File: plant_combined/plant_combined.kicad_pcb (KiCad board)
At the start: 4 copper layers, 68.6 x 58.4 mm, 72 parts, among them J1 SMA-J-P-H-ST-EM1, J2 PJ-002AH, J3 Conn_01x02, U1 SI5351A-B-GT, U10 ZXBM5210-SP-13, U2 OLED_DISP, U3 TDC7200PWR, U4 LMV7219M7, U5 74AC14SC, U6 ESD7002, U7 NCV8163ASN330T1G, U8 PicoW, U9 AP62200WU-7, Y1 Crystal_GND24

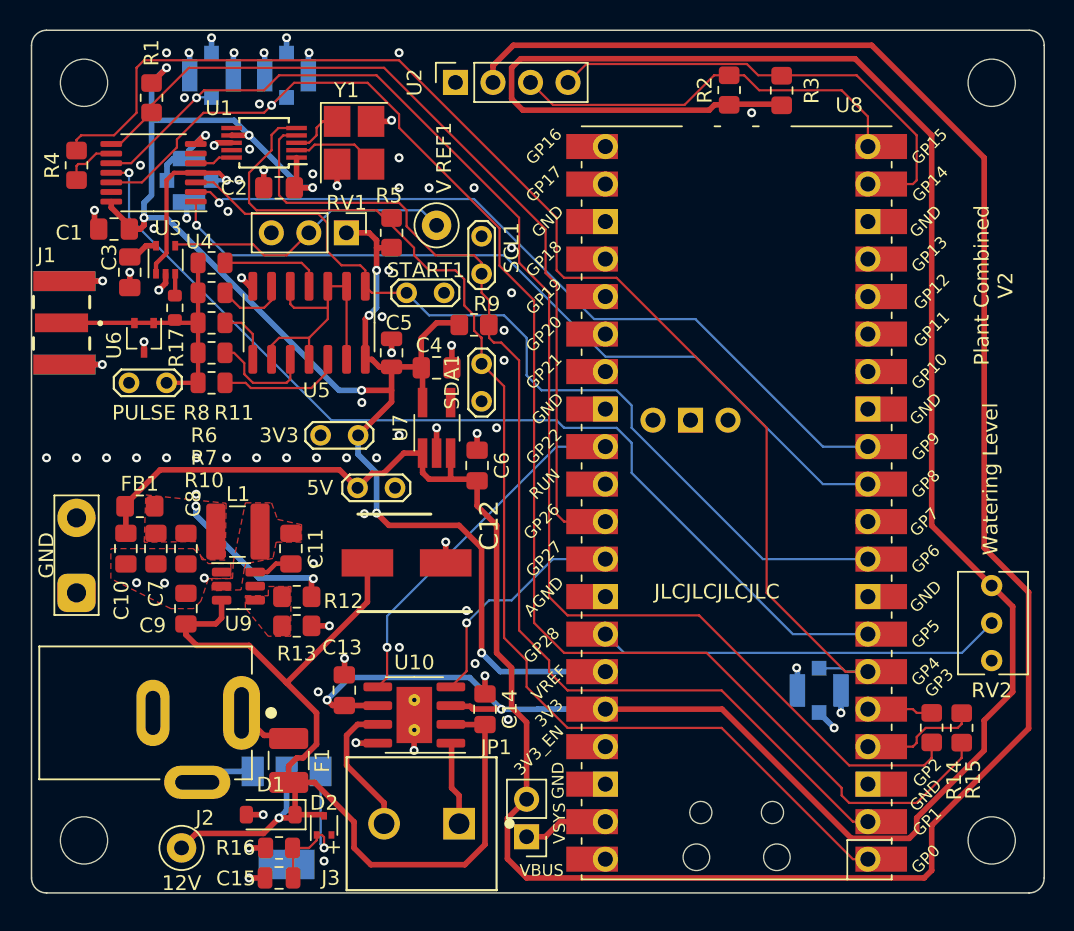
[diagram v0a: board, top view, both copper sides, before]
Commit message: Trying to clean up pulse trace
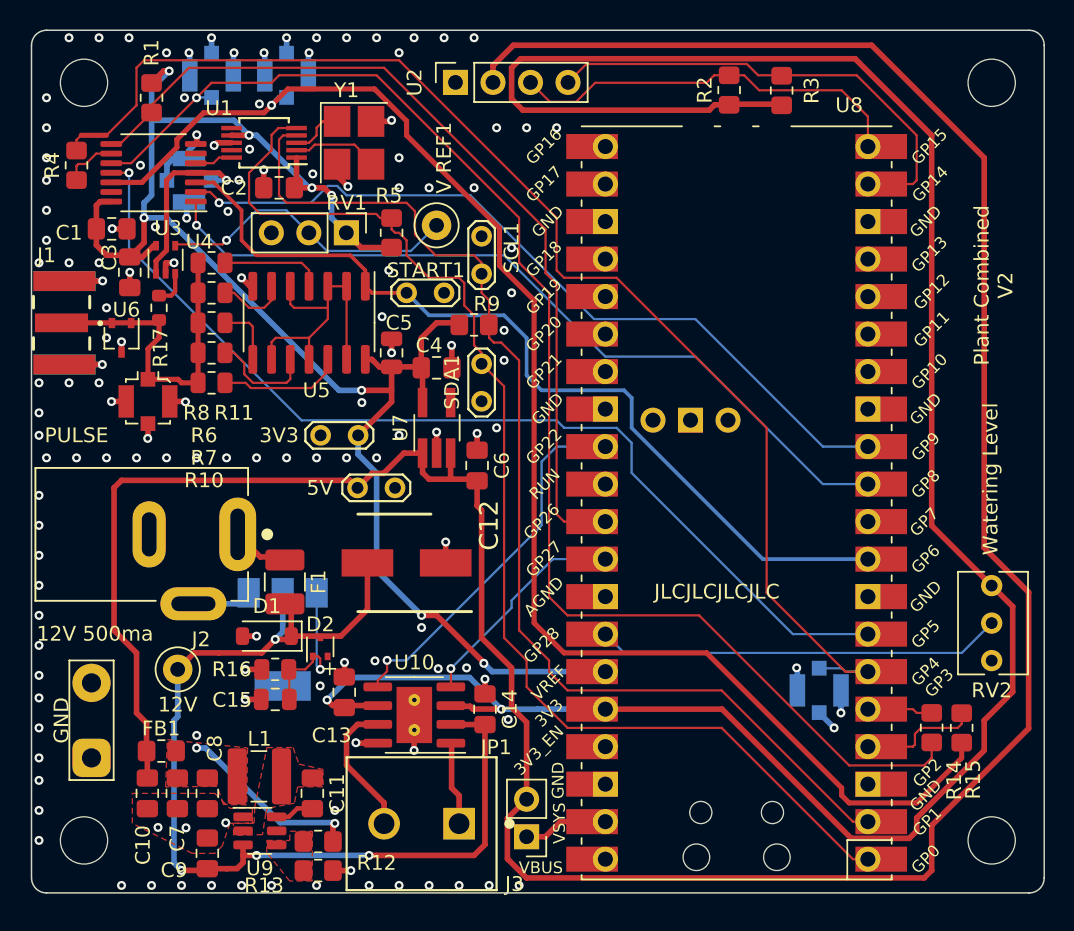
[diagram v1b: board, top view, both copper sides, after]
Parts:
- TP1: footprint Library:TestPoint_2Pads_Pitch2.54mm_Drill1mm -> Connector_Coaxial:U.FL_Molex_MCRF_73412-0110_Vertical
- moved C10 16.6 mm to (44.4, 116.7)
- moved C11 16.6 mm to (55.6, 116.7)
- moved C7 16.6 mm to (46.5, 116.7)
- moved C8 16.6 mm to (48.5, 116.7)
- moved C9 16.6 mm to (48.5, 120.8)
- moved FB1 16.6 mm to (45.4, 113.8)
- moved R12 16.6 mm to (56.0, 120.0)
- moved U9 16.6 mm to (52.0, 119.2)
- moved L1 16.6 mm to (53.5, 115.5)
- moved R13 16.6 mm to (56.0, 121.9)
- moved C15 12.1 mm to (53.1, 110.3)
- moved D1 12.1 mm to (52.5, 106.1)
- moved D2 12.1 mm to (56.1, 106.8)
- moved D3 12.1 mm to (53.6, 106.3)
- moved F1 12.1 mm to (53.7, 102.4)
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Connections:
- TP1 pad 1: GND -> /tdr_sensor/PULSE
- TP1 pad 2: /tdr_sensor/PULSE -> GND
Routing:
- net +5V: track 178.9 -> 197.4 mm
- net +12P: track 75.6 -> 70.0 mm, vias 1 -> 4
- net /tdr_sensor/PULSE: track 19.5 -> 22.5 mm
- net GND: track 62.3 -> 63.9 mm, vias 83 -> 138
- net TDC CSB: track 67.2 -> 68.3 mm
- net /5V_UNFILT: track 11.6 -> 12.8 mm
- net /AIN1: track 16.0 -> 15.1 mm
- net Net-(U4-+): track 1.53 -> 2.42 mm
- net /tdr_sensor/V ref: track 19.7 -> 20.6 mm, vias 0 -> 1
- net /AIN2: track 24.6 -> 25.4 mm
- net +3.3VA: track 116.3 -> 115.6 mm, vias 9 -> 8
- net TRIG: track 52.9 -> 53.7 mm
- net SDA: track 81.5 -> 82.0 mm

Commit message: Final tweak before release
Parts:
- removed R2, R3: 10K, Resistor_SMD:R_0805_2012Metric_Pad1.20x1.40mm_HandSolder
- MOSI1, SCLK1, STOP1, TP1, TP6: footprint Connector_Coaxial:U.FL_Molex_MCRF_73412-0110_Vertical -> Library:HIROSE_U.FL-R-SMT-1(01)
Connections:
- RV2 pad 1: +3.3V -> +3.3VA
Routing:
- net +3.3V: track 156.2 -> 27.5 mm
- net +5V: track 197.4 -> 136.3 mm, vias 0 -> 2
- net +3.3VA: track 115.6 -> 156.9 mm, vias 8 -> 9
- net Net-(U2-SCK): track 27.3 -> 49.5 mm
- net Net-(U2-SDA): track 32.6 -> 43.1 mm
- net GND: track 63.9 -> 56.7 mm, vias 138 -> 127
- net MISO: track 87.2 -> 91.3 mm
- net /AIN2: track 25.4 -> 24.6 mm
- net Net-(U8-GPIO28_ADC2): vias 0 -> 1
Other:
- board text removed: "+"

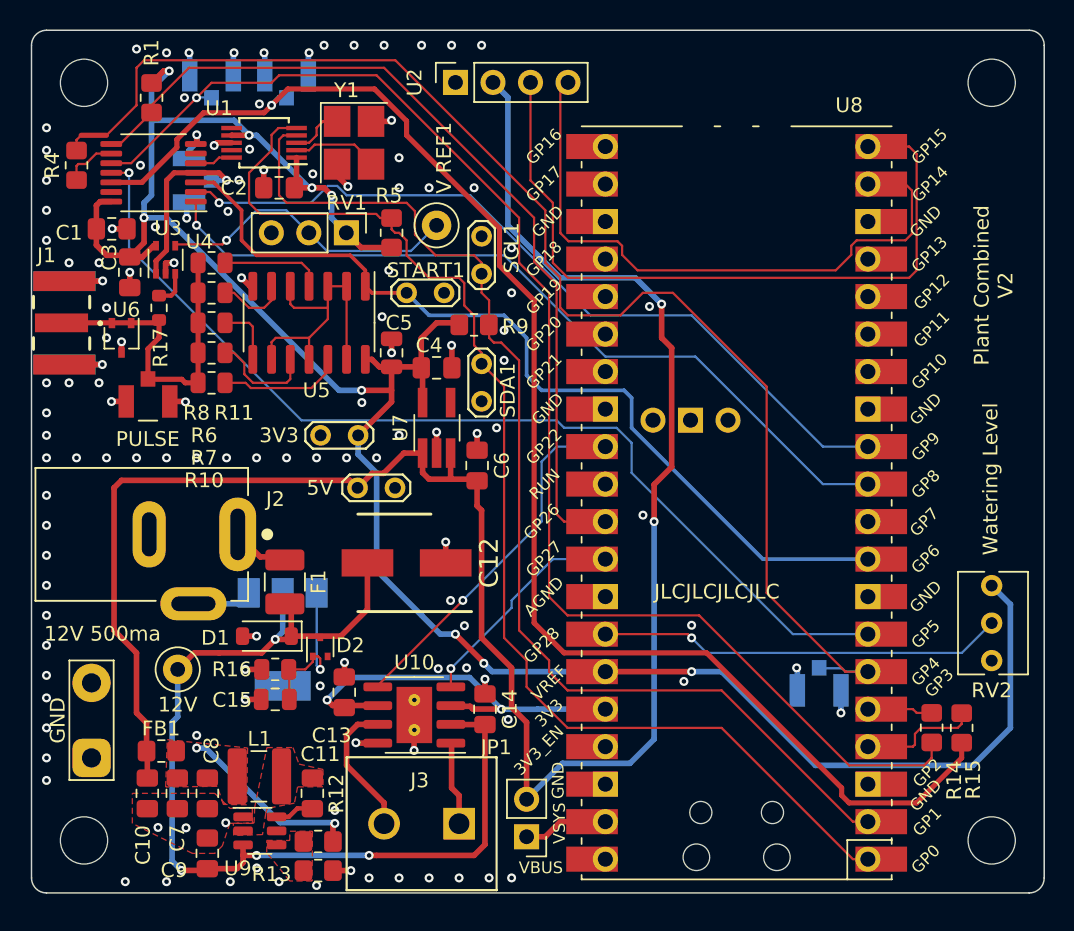
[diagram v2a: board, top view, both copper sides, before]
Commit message: Add pull-up to MISO
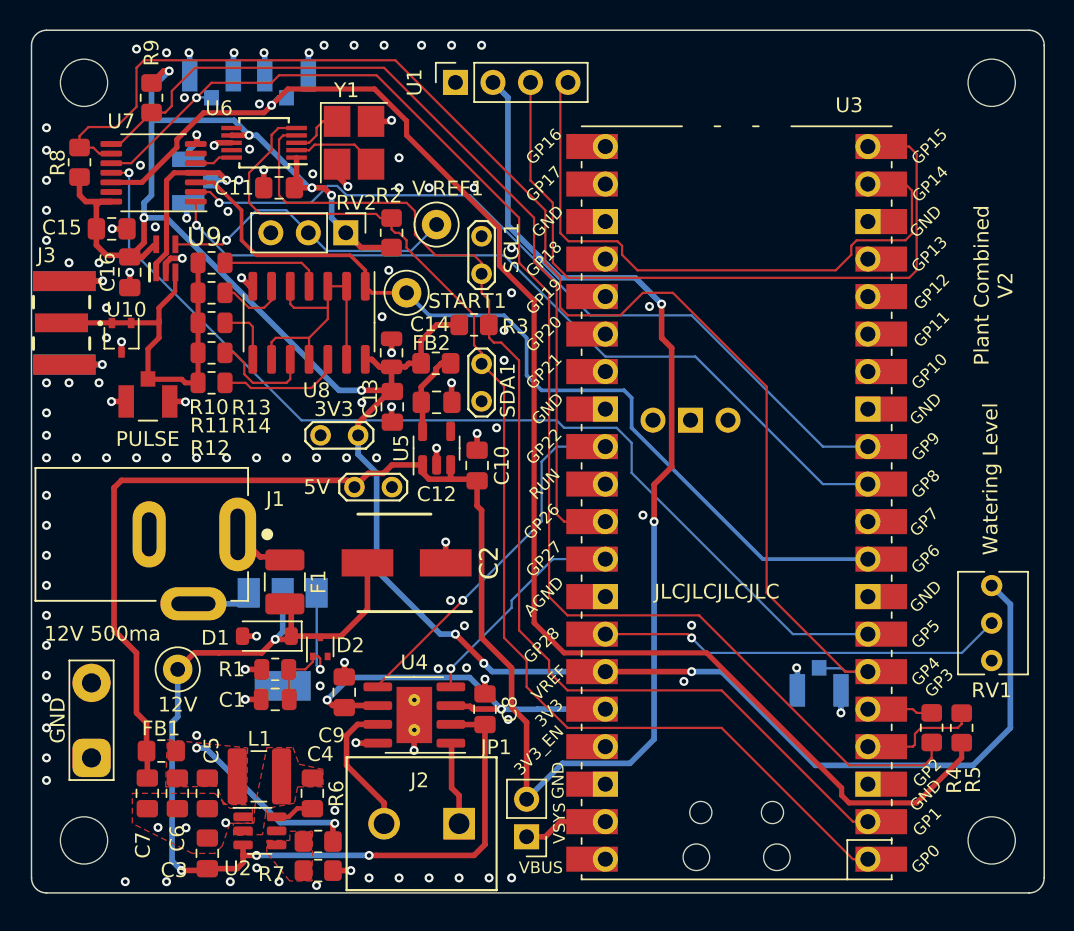
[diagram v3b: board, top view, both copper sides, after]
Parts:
- removed R17: 22, Resistor_SMD:R_0603_1608Metric
- removed the R4 at (39.6, 74.2)
- removed the RV1 at (57.9, 78.7)
- removed the U4 at (45.7, 80.6)
- removed the U7 at (64.0, 91.9)
- added C13: 1uF, Capacitor_SMD:C_0805_2012Metric_Pad1.18x1.45mm_HandSolder, F.Cu at (61.0, 90.5)
- added FB2: ACML-0805-601-T, Resistor_SMD:R_0805_2012Metric_Pad1.20x1.40mm_HandSolder, F.Cu at (64.0, 87.6)
- added R8: 1K, Resistor_SMD:R_0805_2012Metric_Pad1.20x1.40mm_HandSolder, F.Cu at (39.8, 74.0)
- added RV2: 10K, Connector_PinHeader_2.54mm:PinHeader_1x03_P2.54mm_Vertical, F.Cu at (57.9, 78.7)
- added U5: MCP1700T, Package_TO_SOT_SMD:TSOT-23-5, F.Cu at (64.0, 93.3)
- added U9: ADCMP600BKSZ-R2, Library:SOT65P210X110-5N, F.Cu at (45.7, 80.5)
- C10: renamed from C6; value 10uF -> 1uF
- START1: footprint Library:TestPoint_2Pads_Pitch2.54mm_Drill1mm -> TestPoint:TestPoint_Loop_D1.80mm_Drill1.0mm_Beaded
- moved C12 2.34 mm to (64.0, 90.2)
- moved TP3 0.21 mm to (61.0, 96.0)
- moved STOP1 0.07 mm to (47.2, 75.2)
- moved V REF1 0.05 mm to (64.0, 78.2)
- renumbered C15 to C1, C2 to C11, C4 to C12, C5 to C14, C1 to C15, C3 to C16, C12 to C2, C9 to C3, C11 to C4, C8 to C5, C7 to C6, C10 to C7, C14 to C8, C13 to C9, J2 to J1, J3 to J2, J1 to J3, R16 to R1, R8 to R10, R6 to R11, R7 to R12, R10 to R13, R11 to R14, R5 to R2, R9 to R3, R14 to R4, R15 to R5, R12 to R6, R13 to R7, R1 to R9, RV2 to RV1, TP5 to TP1, TP4 to TP2, TP2 to TP4, U2 to U1, U6 to U10, U9 to U2, U8 to U3, U10 to U4, U1 to U6, U3 to U7, U5 to U8
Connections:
- C12 pad 2: +3.3VA -> /tdr_sensor/+3_UNFILTERED
- U7 pad 9: Net-(U3-DOUT) -> MISO
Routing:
- net /tdr_sensor/+3_UNFILTERED: track 0.00 -> 5.83 mm
- net /tdr_sensor/PULSE: track 22.5 -> 26.3 mm
- net Net-(U3-DOUT): track 3.66 -> 0.00 mm
- net Net-(U4-+): track 2.42 -> 0.00 mm
- net MISO: track 91.3 -> 93.4 mm
- net +5V: track 136.3 -> 134.3 mm
- net GND: track 56.7 -> 58.0 mm
- net SDA: track 82.0 -> 80.8 mm
- net +3.3VA: track 156.9 -> 157.6 mm
